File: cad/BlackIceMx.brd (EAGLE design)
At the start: 60 x 50 mm, 6 parts

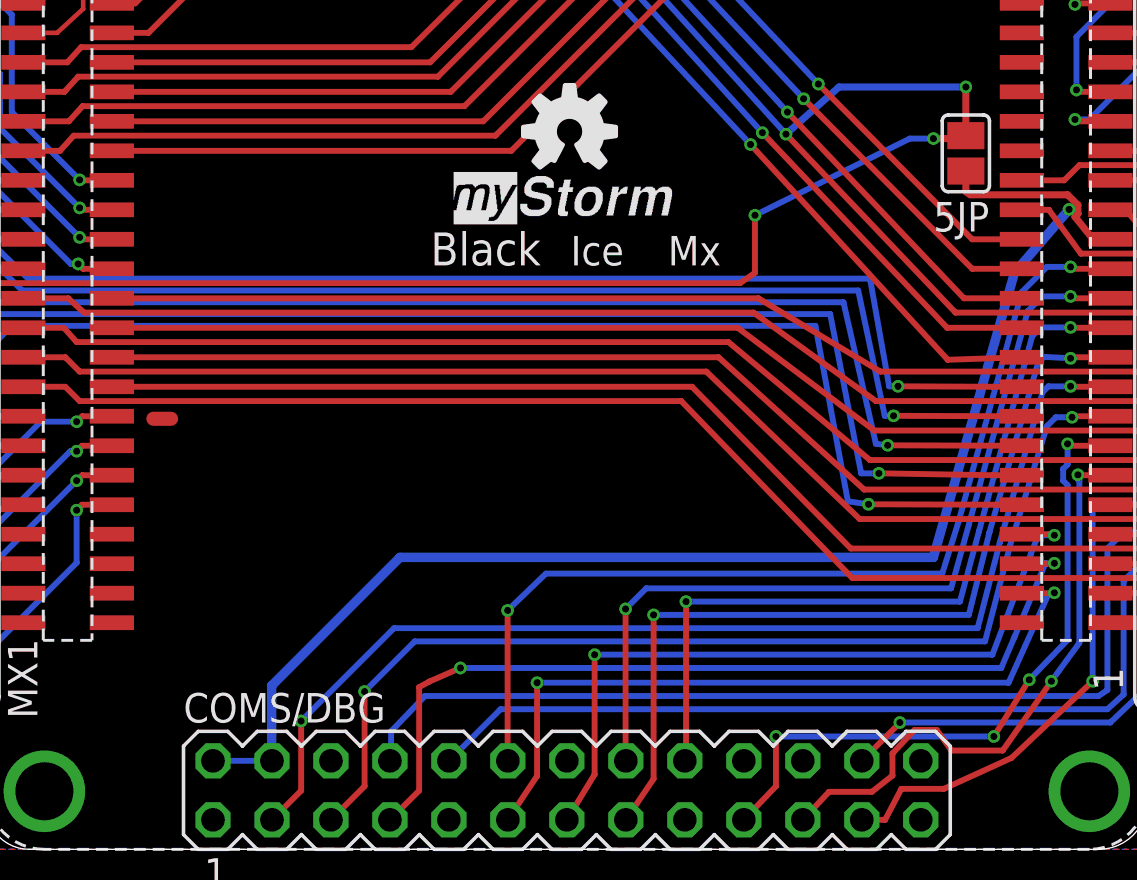
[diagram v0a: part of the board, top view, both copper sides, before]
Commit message: Updated to BlackEdge library
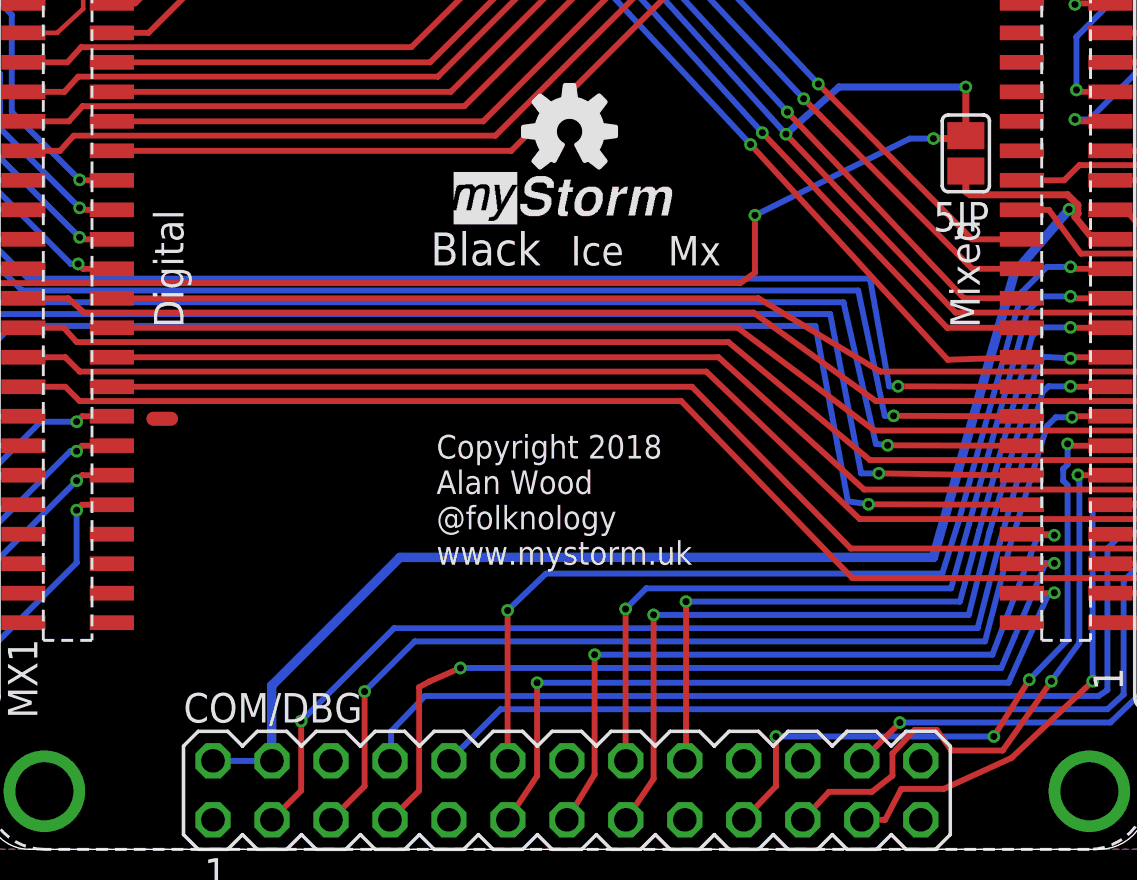
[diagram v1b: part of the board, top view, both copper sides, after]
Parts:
- U$1: device amino:BE-CARRIER-SMD -> BlackEdge:BE-CARRIER-SMD
- renumbered COMS/DBG to COM/DBG
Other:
- board text added: "Copyright 2018 Alan Wood @folknology www.mystorm.uk"
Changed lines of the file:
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@@
 <grid distance="0.0635" unitdist="mm" unit="mm" style="lines" multiple="1" display="no" altdistance="0.025" altunitdist="inch" altunit="inch"/>
 <layers>
-<layer number="1" name="Top" color="4" fill="1" visible="yes" active="yes"/>
+<layer number="1" name="Top" color="0" fill="1" visible="yes" active="yes"/>
 <layer number="2" name="Route2" color="1" fill="3" visible="no" active="no"/>
 <layer number="3" name="Route3" color="4" fill="3" visible="no" active="no"/>
@@
 </polygon>
 <text x="34.3535" y="25.146" size="1.27" layer="25" font="vector" ratio="11">Mx</text>
+<text x="24.384" y="12.2555" size="1.016" layer="21" font="vector" rot="SR0">Copyright 2018
+Alan Wood
+@folknology
+www.mystorm.uk</text>
 </plain>
 <attributes>
@@
 <attribute name="VALUE" x="62.199" y="5.95" size="1.27" layer="27" ratio="10" rot="R90"/>
 </element>
-<element name="U$1" library="amino" package="BE-CARRIER-SMD" value="BE-CARRIERSMD" x="30" y="25" smashed="yes" rot="R90"/>
+<element name="U$1" library="BlackEdge" package="BE-CARRIER-SMD" value="BE-CARRIERSMD" x="30" y="25" smashed="yes" rot="R90"/>
 <element name="5JP" library="jumper" package="SJ" value="" x="47.1805" y="29.972" smashed="yes" rot="SR90">
 <attribute name="NAME" x="45.7835" y="26.6065" size="1.27" layer="25" ratio="10" rot="SR0"/>
 <attribute name="VALUE" x="47.1805" y="30.3721" size="0.02" layer="27" rot="SR90"/>
 </element>
-<element name="COMS/DBG" library="con-lstb" package="MA13-2" value="" x="30" y="2.54">
+<element name="COM/DBG" library="con-lstb" package="MA13-2" value="" x="30" y="2.54">
 <attribute name="MPN" value="" x="30" y="2.54" size="1.778" layer="27" display="off"/>
 <attribute name="OC_NEWARK" value="unknown" x="30" y="2.54" size="1.778" layer="27" display="off"/>
@@
 <wire x1="53.2765" y1="12.954" x2="53.2765" y2="6.858" width="0.254" layer="16"/>
 <wire x1="53.2765" y1="6.858" x2="52.8955" y2="6.604" width="0.254" layer="16"/>
-<contactref element="COMS/DBG" pad="8"/>
+<contactref element="COM/DBG" pad="8"/>
 <wire x1="52.8955" y1="6.604" x2="23.8915" y2="6.604" width="0.254" layer="16"/>
 <wire x1="23.8915" y1="6.604" x2="22.431" y2="5.08" width="0.254" layer="16"/>
@@
 <wire x1="53.975" y1="11.557" x2="53.975" y2="6.6675" width="0.254" layer="16"/>
 <wire x1="53.975" y1="6.6675" x2="53.2765" y2="6.0325" width="0.254" layer="16"/>
-<contactref element="COMS/DBG" pad="10"/>
+<contactref element="COM/DBG" pad="10"/>
 <wire x1="53.2765" y1="6.0325" x2="27.1425" y2="6.0325" width="0.254" layer="16"/>
 <wire x1="27.1425" y1="6.0325" x2="24.92" y2="3.81" width="0.254" layer="16"/>
@@
 <wire x1="49.5935" y1="24.003" x2="46.863" y2="14.097" width="0.254" layer="16"/>
 <wire x1="46.863" y1="14.097" x2="46.1645" y2="11.8745" width="0.254" layer="16"/>
-<contactref element="COMS/DBG" pad="12"/>
+<contactref element="COM/DBG" pad="12"/>
 <wire x1="46.1645" y1="11.8745" x2="29.0985" y2="11.8745" width="0.254" layer="16"/>
 <wire x1="29.0985" y1="11.8745" x2="27.4475" y2="10.287" width="0.254" layer="16"/>
@@
 <via x="51.6255" y="27.559" extent="1-16" drill="0.3" shape="octagon"/>
 <wire x1="51.6255" y1="27.559" x2="52.0065" y2="27.3685" width="0.3048" layer="1"/>
-<contactref element="COMS/DBG" pad="2"/>
-<contactref element="COMS/DBG" pad="4"/>
+<contactref element="COM/DBG" pad="2"/>
+<contactref element="COM/DBG" pad="4"/>
 <wire x1="45.7835" y1="12.573" x2="22.812" y2="12.573" width="0.4064" layer="16"/>
 <wire x1="22.812" y1="12.573" x2="17.2875" y2="7.0485" width="0.4064" layer="16"/>
@@
 <wire x1="49.8475" y1="23.1775" x2="47.3075" y2="13.97" width="0.254" layer="16"/>
 <wire x1="47.3075" y1="13.97" x2="46.5455" y2="11.2395" width="0.254" layer="16"/>
-<contactref element="COMS/DBG" pad="16"/>
+<contactref element="COM/DBG" pad="16"/>
 <wire x1="46.5455" y1="11.2395" x2="33.4165" y2="11.2395" width="0.254" layer="16"/>
 <wire x1="33.4165" y1="11.2395" x2="32.5275" y2="10.3505" width="0.254" layer="16"/>
@@
 <wire x1="50.038" y1="22.098" x2="47.752" y2="13.716" width="0.254" layer="16"/>
 <wire x1="47.752" y1="13.716" x2="46.9265" y2="10.668" width="0.254" layer="16"/>
-<contactref element="COMS/DBG" pad="18"/>
+<contactref element="COM/DBG" pad="18"/>
 <wire x1="46.9265" y1="10.668" x2="35.131" y2="10.668" width="0.254" layer="16"/>
 <via x="35.131" y="10.668" extent="1-16" drill="0.3" shape="octagon"/>
@@
 <wire x1="50.292" y1="20.955" x2="48.1965" y2="13.6525" width="0.254" layer="16"/>
 <wire x1="48.1965" y1="13.6525" x2="47.3075" y2="10.0965" width="0.254" layer="16"/>
-<contactref element="COMS/DBG" pad="15"/>
+<contactref element="COM/DBG" pad="15"/>
 <wire x1="47.3075" y1="10.0965" x2="33.734" y2="10.0965" width="0.254" layer="16"/>
 <via x="33.734" y="10.0965" extent="1-16" drill="0.3" shape="octagon"/>
@@
 <contactref element="MX1" pad="21"/>
 <wire x1="6.595" y1="40.24" x2="3.77" y2="40.24" width="0.6096" layer="1"/>
-<contactref element="COMS/DBG" pad="6"/>
-<contactref element="COMS/DBG" pad="9"/>
-<contactref element="COMS/DBG" pad="14"/>
-<contactref element="COMS/DBG" pad="20"/>
-<contactref element="COMS/DBG" pad="25"/>
+<contactref element="COM/DBG" pad="6"/>
+<contactref element="COM/DBG" pad="9"/>
+<contactref element="COM/DBG" pad="14"/>
+<contactref element="COM/DBG" pad="20"/>
+<contactref element="COM/DBG" pad="25"/>
 </signal>
 <signal name="5V">
@@
 </signal>
 <signal name="!RESET">
-<contactref element="COMS/DBG" pad="13"/>
+<contactref element="COM/DBG" pad="13"/>
 <contactref element="U$1" pad="P$54"/>
 <wire x1="49.595" y1="13.57" x2="50.8825" y2="13.57" width="0.254" layer="1"/>
@@
 </signal>
 <signal name="SWDIO">
-<contactref element="COMS/DBG" pad="11"/>
+<contactref element="COM/DBG" pad="11"/>
 <contactref element="U$1" pad="P$52"/>
 <wire x1="49.595" y1="11.03" x2="50.9715" y2="11.03" width="0.254" layer="1"/>
@@
 </signal>
 <signal name="SWCLK">
-<contactref element="COMS/DBG" pad="7"/>
+<contactref element="COM/DBG" pad="7"/>
 <contactref element="U$1" pad="P$53"/>
 <wire x1="49.595" y1="12.3" x2="50.8445" y2="12.3" width="0.254" layer="1"/>
@@
 </signal>
 <signal name="DONE">
-<contactref element="COMS/DBG" pad="22"/>
+<contactref element="COM/DBG" pad="22"/>
 </signal>
 <signal name="SCL">
-<contactref element="COMS/DBG" pad="5"/>
+<contactref element="COM/DBG" pad="5"/>
 <contactref element="U$1" pad="P$83"/>
 <wire x1="53.405" y1="18.65" x2="51.797" y2="18.65" width="0.254" layer="1"/>
@@
 </signal>
 <signal name="SDA">
-<contactref element="COMS/DBG" pad="3"/>
+<contactref element="COM/DBG" pad="3"/>
 <contactref element="U$1" pad="P$84"/>
 <wire x1="53.405" y1="19.92" x2="51.708" y2="19.92" width="0.254" layer="1"/>
@@
 </signal>
 <signal name="ESCK">
-<contactref element="COMS/DBG" pad="23"/>
+<contactref element="COM/DBG" pad="23"/>
 <contactref element="U$1" pad="P$80"/>
 <wire x1="53.405" y1="14.84" x2="54.845" y2="14.84" width="0.254" layer="1"/>
@@
 </signal>
 <signal name="EMISO">
-<contactref element="COMS/DBG" pad="21"/>
+<contactref element="COM/DBG" pad="21"/>
 <contactref element="U$1" pad="P$81"/>
 <wire x1="53.405" y1="16.11" x2="52.1525" y2="16.11" width="0.254" layer="1"/>
@@
 </signal>
 <signal name="EMOSI">
-<contactref element="COMS/DBG" pad="19"/>
+<contactref element="COM/DBG" pad="19"/>
 <contactref element="U$1" pad="P$82"/>
 <wire x1="53.405" y1="17.38" x2="51.6445" y2="17.38" width="0.254" layer="1"/>
@@
 </signal>
 <signal name="!ESS">
-<contactref element="COMS/DBG" pad="24"/>
+<contactref element="COM/DBG" pad="24"/>
 <contactref element="U$1" pad="P$77"/>
 <wire x1="53.405" y1="11.03" x2="54.845" y2="11.03" width="0.254" layer="1"/>
@@
 </board>
 </drawing>
+<compatibility>
+<note version="6.3" minversion="6.2.2" severity="warning">
+Since Version 6.2.2 text objects can contain more than one line,
+which will not be processed correctly with this version.
+</note>
+</compatibility>
 </eagle>
